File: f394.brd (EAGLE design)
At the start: 9.8 x 7.4 mm, 4 parts

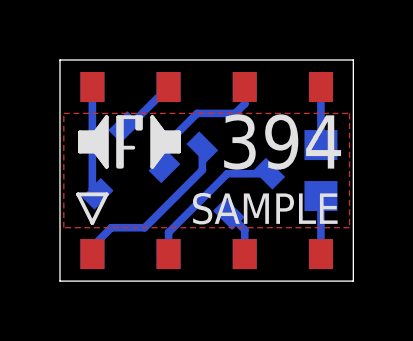
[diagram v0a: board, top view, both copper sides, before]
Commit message: Update F394 to use PMP4201Y
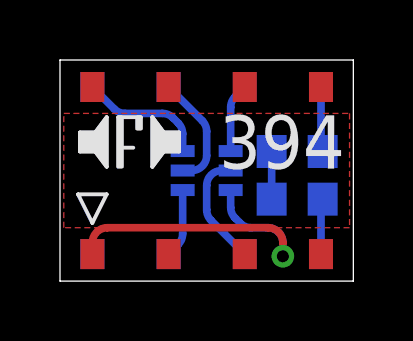
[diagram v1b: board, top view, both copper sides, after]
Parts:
- removed VT2: 2SC3324, transistors-npn:SOT23-R
- added R2: (no value), resistors:R-0603
- 394: value SAMPLE -> (none)
- VT1: value 2SC3324 -> PMP4201Y; device transistors-npn:SOT23-R -> transistors-npn:SOT363_PHILIPS
- moved R1 1.24 mm to (8.10, 2.86), turned to 0 degrees
- moved VT1 0.63 mm to (5.08, 3.81), turned to 90 degrees
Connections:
- net N$2 renamed B1
- removed net N$5: 394.B7, 394.T7, VT2.1
- removed net N$9 (its old number): 394.B5, 394.T5, R1.2
- new net B2: 394.B7, 394.T7, VT1.2
- new net N$10: 394.B5, 394.T5, R2.2
- new net N$7: R1.2, R2.1
- net N$1: now also VT1.6; no longer VT1.3
- net N$3: now also VT1.4; no longer VT2.2
- net N$4: now also VT1.3; no longer VT2.3
- net N$6: now also VT1.5; no longer VT1.2
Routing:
- net N$1: track 5.73 -> 10.9 mm, vias 0 -> 1
- net B2: track 0.00 -> 3.79 mm
- net B1: track 4.89 -> 2.30 mm
- net N$3: track 4.53 -> 2.30 mm
- net N$6: track 1.55 -> 3.79 mm
- net N$10: track 0.00 -> 2.17 mm
- net N$5: track 2.03 -> 0.00 mm
- net N$9 (its old number): track 1.93 -> 0.00 mm
- net N$7: track 0.00 -> 1.59 mm
- net N$4: track 3.64 -> 4.26 mm
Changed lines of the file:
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@@
 <?xml version="1.0" encoding="utf-8"?>
 <!DOCTYPE eagle SYSTEM "eagle.dtd">
-<eagle version="7.5.0">
+<eagle version="7.5.1">
 <drawing>
 <settings>
@@
 </autorouter>
 <elements>
-<element name="394" library="module-footprints" package="BA3760X8" value="SAMPLE" x="0" y="0"/>
-<element name="VT1" library="transistors-npn" package="SOT23-R" value="2SC3324" x="5.715" y="3.81" smashed="yes" rot="MR315">
-<attribute name="MOUSER" value="757-2SC3324BLTE85LF" x="5.715" y="3.81" size="1.778" layer="28" rot="MR315" display="off"/>
-</element>
-<element name="VT2" library="transistors-npn" package="SOT23-R" value="2SC3324" x="2.2225" y="3.81" smashed="yes" rot="MR225">
-<attribute name="MOUSER" value="757-2SC3324BLTE85LF" x="2.2225" y="3.81" size="1.778" layer="28" rot="MR225" display="off"/>
-</element>
-<element name="R1" library="resistors" package="R-0603" value="" x="8.89" y="3.81" smashed="yes" rot="MR90"/>
+<element name="394" library="module-footprints" package="BA3760X8" value="" x="0" y="0"/>
+<element name="R1" library="resistors" package="R-0603" value="" x="8.09625" y="2.8575" smashed="yes" rot="MR0"/>
+<element name="R2" library="resistors" package="R-0603" value="" x="8.09625" y="4.445" smashed="yes" rot="MR180"/>
+<element name="VT1" library="transistors-npn" package="SOT363_PHILIPS" value="PMP4201Y" x="5.08" y="3.81" smashed="yes" rot="MR90"/>
 </elements>
 <signals>
@@
 <contactref element="394" pad="B1"/>
 <contactref element="394" pad="T1"/>
-<contactref element="VT1" pad="3"/>
-<wire x1="4.937184375" y1="4.587815625" x2="4.937184375" y2="3.825934375" width="0.254" layer="16"/>
-<wire x1="4.937184375" y1="3.825934375" x2="3.01625" y2="1.905" width="0.254" layer="16"/>
-<wire x1="3.01625" y1="1.905" x2="1.905" y2="1.905" width="0.254" layer="16"/>
-<wire x1="1.27" y1="1.025" x2="1.27" y2="1.27" width="0.254" layer="16"/>
-<wire x1="1.27" y1="1.27" x2="1.905" y2="1.905" width="0.254" layer="16"/>
+<contactref element="VT1" pad="6"/>
+<wire x1="5.88" y1="3.16" x2="5.88" y2="2.58210625" width="0.254" layer="16"/>
+<wire x1="5.88" y1="2.58210625" x2="6.026446875" y2="2.228553125" width="0.254" layer="16" curve="45"/>
+<wire x1="6.026446875" y1="2.228553125" x2="6.203553125" y2="2.051446875" width="0.254" layer="16"/>
+<wire x1="6.203553125" y1="2.051446875" x2="6.55710625" y2="1.905" width="0.254" layer="16" curve="45"/>
+<wire x1="6.55710625" y1="1.905" x2="7.12" y2="1.905" width="0.254" layer="16"/>
+<wire x1="7.12" y1="1.905" x2="7.62" y2="1.405" width="0.254" layer="16" curve="-90"/>
+<wire x1="7.62" y1="1.405" x2="7.62" y2="0.9525" width="0.254" layer="16"/>
+<via x="7.62" y="0.9525" extent="1-16" drill="0.4"/>
+<wire x1="7.62" y1="0.9525" x2="7.62" y2="1.405" width="0.254" layer="1"/>
+<wire x1="7.62" y1="1.405" x2="7.12" y2="1.905" width="0.254" layer="1" curve="90"/>
+<wire x1="7.12" y1="1.905" x2="1.77" y2="1.905" width="0.254" layer="1"/>
+<wire x1="1.77" y1="1.905" x2="1.27" y2="1.405" width="0.254" layer="1" curve="90"/>
+<wire x1="1.27" y1="1.405" x2="1.27" y2="1.025" width="0.254" layer="1"/>
 <wire x1="1.27" y1="1.025" x2="1.27" y2="1.025" width="0" layer="19" extent="1-16"/>
 </signal>
-<signal name="N$2">
-<contactref element="VT1" pad="1"/>
+<signal name="B1">
 <contactref element="394" pad="B2"/>
 <contactref element="394" pad="T2"/>
-<wire x1="3.81" y1="1.025" x2="3.81" y2="1.74625" width="0.254" layer="16"/>
-<wire x1="3.81" y1="1.74625" x2="5.76768125" y2="3.70393125" width="0.254" layer="16"/>
-<wire x1="5.76768125" y1="3.70393125" x2="7.164571875" y2="3.70393125" width="0.254" layer="16"/>
+<contactref element="VT1" pad="1"/>
+<wire x1="4.28" y1="3.16" x2="4.28" y2="1.70210625" width="0.254" layer="16"/>
+<wire x1="4.28" y1="1.70210625" x2="4.133553125" y2="1.348553125" width="0.254" layer="16" curve="-45"/>
+<wire x1="4.133553125" y1="1.348553125" x2="3.81" y2="1.025" width="0.254" layer="16"/>
 <wire x1="3.81" y1="1.025" x2="3.81" y2="1.025" width="0" layer="19" extent="1-16"/>
 </signal>
@@
 <contactref element="394" pad="B6"/>
 <contactref element="394" pad="T6"/>
-<contactref element="VT2" pad="2"/>
-<wire x1="3.672071875" y1="3.916065625" x2="3.672071875" y2="4.624571875" width="0.254" layer="16"/>
-<wire x1="3.672071875" y1="4.624571875" x2="4.7625" y2="5.715" width="0.254" layer="16"/>
-<wire x1="4.7625" y1="5.715" x2="6.0325" y2="5.715" width="0.254" layer="16"/>
-<wire x1="6.0325" y1="5.715" x2="6.35" y2="6.0325" width="0.254" layer="16"/>
-<wire x1="6.35" y1="6.0325" x2="6.35" y2="6.595" width="0.254" layer="16"/>
+<contactref element="VT1" pad="4"/>
+<wire x1="5.88" y1="4.46" x2="5.88" y2="5.91789375" width="0.254" layer="16"/>
+<wire x1="5.88" y1="5.91789375" x2="6.026446875" y2="6.271446875" width="0.254" layer="16" curve="-45"/>
+<wire x1="6.026446875" y1="6.271446875" x2="6.35" y2="6.595" width="0.254" layer="16"/>
 <wire x1="6.35" y1="6.595" x2="6.35" y2="6.595" width="0" layer="19" extent="1-16"/>
 </signal>
@@
 <contactref element="394" pad="B8"/>
 <contactref element="394" pad="T8"/>
-<contactref element="VT2" pad="3"/>
-<wire x1="1.27" y1="6.595" x2="1.27" y2="3.206865625" width="0.254" layer="16"/>
-<wire x1="1.27" y1="3.206865625" x2="1.444684375" y2="3.03218125" width="0.254" layer="16"/>
+<contactref element="VT1" pad="3"/>
+<wire x1="4.28" y1="4.46" x2="4.28" y2="5.03789375" width="0.254" layer="16"/>
+<wire x1="4.28" y1="5.03789375" x2="4.133553125" y2="5.391446875" width="0.254" layer="16" curve="45"/>
+<wire x1="4.133553125" y1="5.391446875" x2="3.956446875" y2="5.568553125" width="0.254" layer="16"/>
+<wire x1="3.956446875" y1="5.568553125" x2="3.60289375" y2="5.715" width="0.254" layer="16" curve="45"/>
+<wire x1="3.60289375" y1="5.715" x2="2.35710625" y2="5.715" width="0.254" layer="16"/>
+<wire x1="2.35710625" y1="5.715" x2="2.003553125" y2="5.861446875" width="0.254" layer="16" curve="-45"/>
+<wire x1="2.003553125" y1="5.861446875" x2="1.27" y2="6.595" width="0.254" layer="16"/>
 <wire x1="1.27" y1="6.595" x2="1.27" y2="6.595" width="0" layer="19" extent="1-16"/>
 </signal>
-<signal name="N$5">
+<signal name="B2">
 <contactref element="394" pad="T7"/>
 <contactref element="394" pad="B7"/>
-<contactref element="VT2" pad="1"/>
-<wire x1="2.32856875" y1="5.25956875" x2="2.47456875" y2="5.25956875" width="0.254" layer="16"/>
-<wire x1="2.47456875" y1="5.25956875" x2="3.81" y2="6.595" width="0.254" layer="16"/>
+<contactref element="VT1" pad="2"/>
+<wire x1="4.28" y1="3.81" x2="4.58" y2="3.81" width="0.254" layer="16"/>
+<wire x1="4.58" y1="3.81" x2="5.08" y2="4.31" width="0.254" layer="16" curve="90"/>
+<wire x1="5.08" y1="4.31" x2="5.08" y2="5.11789375" width="0.254" layer="16"/>
+<wire x1="5.08" y1="5.11789375" x2="4.933553125" y2="5.471446875" width="0.254" layer="16" curve="45"/>
+<wire x1="4.933553125" y1="5.471446875" x2="3.81" y2="6.595" width="0.254" layer="16"/>
 <wire x1="3.81" y1="6.595" x2="3.81" y2="6.595" width="0" layer="19" extent="1-16"/>
-</signal>
-<signal name="N$9">
-<contactref element="R1" pad="2"/>
-<contactref element="394" pad="B5"/>
-<contactref element="394" pad="T5"/>
-<wire x1="8.89" y1="4.66" x2="8.89" y2="6.595" width="0.254" layer="16"/>
-<wire x1="8.89" y1="6.595" x2="8.89" y2="6.595" width="0" layer="19" extent="1-16"/>
 </signal>
 <signal name="N$6">
 <contactref element="394" pad="B3"/>
 <contactref element="394" pad="T3"/>
-<contactref element="VT1" pad="2"/>
-<wire x1="5.82106875" y1="2.360428125" x2="6.35" y2="1.831496875" width="0.254" layer="16"/>
-<wire x1="6.35" y1="1.831496875" x2="6.35" y2="1.025" width="0.254" layer="16"/>
+<contactref element="VT1" pad="5"/>
+<wire x1="5.88" y1="3.81" x2="5.58" y2="3.81" width="0.254" layer="16"/>
+<wire x1="5.58" y1="3.81" x2="5.08" y2="3.31" width="0.254" layer="16" curve="90"/>
+<wire x1="5.08" y1="3.31" x2="5.08" y2="2.50210625" width="0.254" layer="16"/>
+<wire x1="5.08" y1="2.50210625" x2="5.226446875" y2="2.148553125" width="0.254" layer="16" curve="45"/>
+<wire x1="5.226446875" y1="2.148553125" x2="6.35" y2="1.025" width="0.254" layer="16"/>
 <wire x1="6.35" y1="1.025" x2="6.35" y2="1.025" width="0" layer="19" extent="1-16"/>
-</signal>
-<signal name="N$7">
-<contactref element="394" pad="T4"/>
-<contactref element="394" pad="B4"/>
-<contactref element="R1" pad="1"/>
-<wire x1="8.89" y1="2.96" x2="8.89" y2="1.025" width="0.254" layer="16"/>
-<wire x1="8.89" y1="1.025" x2="8.89" y2="1.025" width="0" layer="19" extent="1-16"/>
 </signal>
 <signal name="N$8">
@@
 </polygon>
 </signal>
+<signal name="N$7">
+<contactref element="R1" pad="2"/>
+<contactref element="R2" pad="1"/>
+<wire x1="7.24625" y1="2.8575" x2="7.24625" y2="4.445" width="0.254" layer="16"/>
+</signal>
+<signal name="N$9">
+<contactref element="394" pad="T4"/>
+<contactref element="394" pad="B4"/>
+<contactref element="R1" pad="1"/>
+<wire x1="8.89" y1="1.025" x2="8.89" y2="2.80125" width="0.254" layer="16"/>
+<wire x1="8.89" y1="2.80125" x2="8.94625" y2="2.8575" width="0.254" layer="16"/>
+<wire x1="8.89" y1="1.025" x2="8.89" y2="1.025" width="0" layer="19" extent="1-16"/>
+</signal>
+<signal name="N$10">
+<contactref element="R2" pad="2"/>
+<contactref element="394" pad="B5"/>
+<contactref element="394" pad="T5"/>
+<wire x1="8.89" y1="6.595" x2="8.89" y2="4.50125" width="0.254" layer="16"/>
+<wire x1="8.89" y1="4.50125" x2="8.94625" y2="4.445" width="0.254" layer="16"/>
+<wire x1="8.89" y1="6.595" x2="8.89" y2="6.595" width="0" layer="19" extent="1-16"/>
+</signal>
 </signals>

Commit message: Change PTC positioning
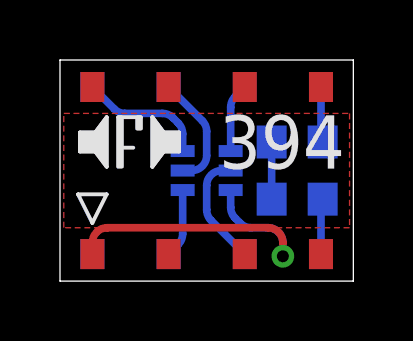
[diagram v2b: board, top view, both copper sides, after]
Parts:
- moved R2 0.32 mm to (8.10, 4.76)
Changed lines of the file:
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@@
 <element name="394" library="module-footprints" package="BA3760X8" value="" x="0" y="0"/>
 <element name="R1" library="resistors" package="R-0603" value="" x="8.09625" y="2.8575" smashed="yes" rot="MR0"/>
-<element name="R2" library="resistors" package="R-0603" value="" x="8.09625" y="4.445" smashed="yes" rot="MR180"/>
+<element name="R2" library="resistors" package="R-0603" value="" x="8.09625" y="4.7625" smashed="yes" rot="MR180"/>
 <element name="VT1" library="transistors-npn" package="SOT363_PHILIPS" value="PMP4201Y" x="5.08" y="3.81" smashed="yes" rot="MR90"/>
 </elements>
@@
 <contactref element="R1" pad="2"/>
 <contactref element="R2" pad="1"/>
-<wire x1="7.24625" y1="2.8575" x2="7.24625" y2="4.445" width="0.254" layer="16"/>
+<wire x1="7.24625" y1="2.8575" x2="7.24625" y2="4.7625" width="0.254" layer="16"/>
 </signal>
 <signal name="N$9">
@@
 <contactref element="394" pad="T5"/>
 <wire x1="8.89" y1="6.595" x2="8.89" y2="4.50125" width="0.254" layer="16"/>
-<wire x1="8.89" y1="4.50125" x2="8.94625" y2="4.445" width="0.254" layer="16"/>
+<wire x1="8.89" y1="4.50125" x2="8.94625" y2="4.7625" width="0.254" layer="16"/>
 <wire x1="8.89" y1="6.595" x2="8.89" y2="6.595" width="0" layer="19" extent="1-16"/>
 </signal>
